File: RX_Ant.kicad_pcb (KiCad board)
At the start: 2 copper layers, 100 x 100 mm, 1630 parts, among them J1 CONN_COAXIAL, J10 CONN_COAXIAL, J11 CONN_COAXIAL, J12 CONN_01X05, J13 CONN_COAXIAL, J14 Conn_01x07, J15 CONN_COAXIAL, J16 CONN_01X01, J17 CONN_01X01, J18 CONN_01X01, J19 CONN_01X01, J2 CONN_COAXIAL, J20 CONN_01X01, J21 CONN_01X01, J22 CONN_01X01, J23 CONN_01X01, J24 CONN_COAXIAL, J25 CONN_COAXIAL, J26 CONN_COAXIAL, J27 CONN_COAXIAL, J28 CONN_COAXIAL, J29 CONN_COAXIAL, J3 CONN_COAXIAL, J30 CONN_COAXIAL, J31 CONN_COAXIAL, J32 CONN_COAXIAL, J34 CONN_COAXIAL, J35 CONN_COAXIAL, J37 CONN_COAXIAL, J4 CONN_COAXIAL, J5 CONN_COAXIAL, J6 CONN_COAXIAL, J8 CONN_COAXIAL, J9 CONN_COAXIAL

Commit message: minor errors fixed, sma edge should be changed
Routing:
- net Net-(J2-Pad1): track 16.4 -> 18.9 mm
- net Net-(J15-Pad1): track 25.4 -> 27.9 mm
- net Net-(J10-Pad1): track 17.3 -> 19.8 mm
- net Net-(J29-Pad1): track 28.0 -> 25.6 mm
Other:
- board text added: "(master)"
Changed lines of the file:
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@@
     (area 19.924999 24.924999 120.075001 125.075001)
     (thickness 1.6)
-    (drawings 35)
-    (tracks 1426)
+    (drawings 37)
+    (tracks 1428)
     (zones 0)
     (modules 1630)
@@
   )
   (setup
-    (last_trace_width 0.25)
+    (last_trace_width 2)
     (user_trace_width 0.5)
     (user_trace_width 1)
@@
     )
   )
+  (gr_text "(master)" (at 33 82.8) (layer F.SilkS)
+    (effects (font (size 1 1) (thickness 0.25) italic))
+  )
+  (gr_text "(master)" (at 34.2 34) (layer F.SilkS)
+    (effects (font (size 1 1) (thickness 0.25) italic))
+  )
   (gr_text "(HPF in)" (at 108 83 180) (layer F.SilkS)
     (effects (font (size 1 1) (thickness 0.25)))
@@
   (segment (start 80 86.65) (end 88.65 86.65) (width 2) (layer F.Cu) (net 2))
   (segment (start 88.65 86.65) (end 101.65 86.65) (width 2) (layer F.Cu) (net 2))
-  (segment (start 75 122.4) (end 75 120) (width 1) (layer F.Cu) (net 3))
+  (segment (start 75 122.5) (end 75 120) (width 2) (layer B.Cu) (net 3))
   (segment (start 75 120) (end 75 104.54) (width 2) (layer B.Cu) (net 3))
   (segment (start 75 104.54) (end 79.46 100.08) (width 2) (layer B.Cu) (net 3))
   (segment (start 84.54 100.08) (end 79.46 100.08) (width 2) (layer B.Cu) (net 3))
+  (segment (start 40 72.5) (end 40 70) (width 2) (layer B.Cu) (net 4))
   (segment (start 40 70) (end 40 65) (width 2) (layer B.Cu) (net 4))
   (segment (start 40 59) (end 40 65) (width 2.9) (layer B.Cu) (net 4))
   (segment (start 40 59) (end 43.5 55.5) (width 2.9) (layer B.Cu) (net 4))
   (segment (start 44 55.5) (end 43.5 55.5) (width 2.9) (layer B.Cu) (net 4))
+  (segment (start 100 72.5) (end 100 70) (width 2) (layer B.Cu) (net 5))
   (segment (start 100 70) (end 100 65) (width 2) (layer B.Cu) (net 5))
   (segment (start 100 61) (end 100 65) (width 2.9) (layer B.Cu) (net 5))
@@
   (segment (start 106.54 51.5) (end 46 51.5) (width 1) (layer F.Cu) (net 12))
   (via (at 46 51.5) (size 0.6) (drill 0.4) (layers F.Cu B.Cu) (net 12))
+  (segment (start 72.5 77.5) (end 72.5 80) (width 2) (layer B.Cu) (net 13))
   (segment (start 69.04 98.04) (end 70.46 98.04) (width 2) (layer B.Cu) (net 13))
   (segment (start 72.5 96) (end 72.5 80) (width 2) (layer B.Cu) (net 13))
@@
   (segment (start 60 93) (end 66.46 93) (width 1) (layer F.Cu) (net 20))
   (segment (start 66.46 93) (end 69.04 90.42) (width 1) (layer F.Cu) (net 20))
-  (segment (start 90 122.4) (end 90 120) (width 1) (layer F.Cu) (net 21))
   (segment (start 91.46 100.08) (end 96.54 100.08) (width 2) (layer B.Cu) (net 21))
   (segment (start 90 120) (end 90 101.54) (width 2) (layer B.Cu) (net 21))
   (segment (start 90 101.54) (end 91.46 100.08) (width 2) (layer B.Cu) (net 21))
-  (segment (start 70 72.4) (end 70 70) (width 2) (layer F.Cu) (net 22))
+  (segment (start 70 72.5) (end 70 70) (width 2) (layer B.Cu) (net 22))
   (segment (start 70 70) (end 70 65.2) (width 2) (layer B.Cu) (net 22))
   (segment (start 70 65.2) (end 70 56.5) (width 2.9) (layer B.Cu) (net 22))
   (segment (start 70 56.5) (end 69 55.5) (width 2) (layer B.Cu) (net 22))
-  (segment (start 105 122.4) (end 105 120) (width 1) (layer F.Cu) (net 23))
+  (segment (start 105 122.5) (end 105 120) (width 2) (layer B.Cu) (net 23))
   (segment (start 103.46 100.08) (end 108.54 100.08) (width 2) (layer B.Cu) (net 23))
   (segment (start 105 120) (end 105 101.62) (width 2) (layer B.Cu) (net 23))
   (segment (start 105 101.62) (end 103.46 100.08) (width 2) (layer B.Cu) (net 23))
+  (segment (start 60 122.5) (end 60 120) (width 2) (layer B.Cu) (net 24))
   (segment (start 60 120) (end 60 104.54) (width 2) (layer B.Cu) (net 24))
   (segment (start 60 104.54) (end 63.96 100.58) (width 2) (layer B.Cu) (net 24))
   (segment (start 63.96 100.58) (end 69.04 100.58) (width 2) (layer B.Cu) (net 24))
-  (segment (start 60 122.4) (end 60 120) (width 1) (layer F.Cu) (net 24))
-  (segment (start 100 77.5) (end 100 80) (width 1) (layer B.Cu) (net 25))
+  (segment (start 100 77.5) (end 100 80) (width 2) (layer B.Cu) (net 25))
   (segment (start 100 80) (end 100 97.54) (width 2) (layer B.Cu) (net 25))
   (segment (start 84.54 97.54) (end 79.46 97.54) (width 2) (layer B.Cu) (net 25))
@@
   (segment (start 100 97.54) (end 103.46 97.54) (width 2) (layer B.Cu) (net 25))
   (segment (start 91.46 97.54) (end 96.54 97.54) (width 2) (layer B.Cu) (net 25))
-  (segment (start 70 27.5) (end 70 30) (width 1) (layer B.Cu) (net 26))
+  (segment (start 70 27.5) (end 70 30) (width 2) (layer B.Cu) (net 26))
   (segment (start 75 41.3) (end 70 36.3) (width 2.9) (layer B.Cu) (net 26))
   (segment (start 70 36.3) (end 70 35) (width 2.9) (layer B.Cu) (net 26))

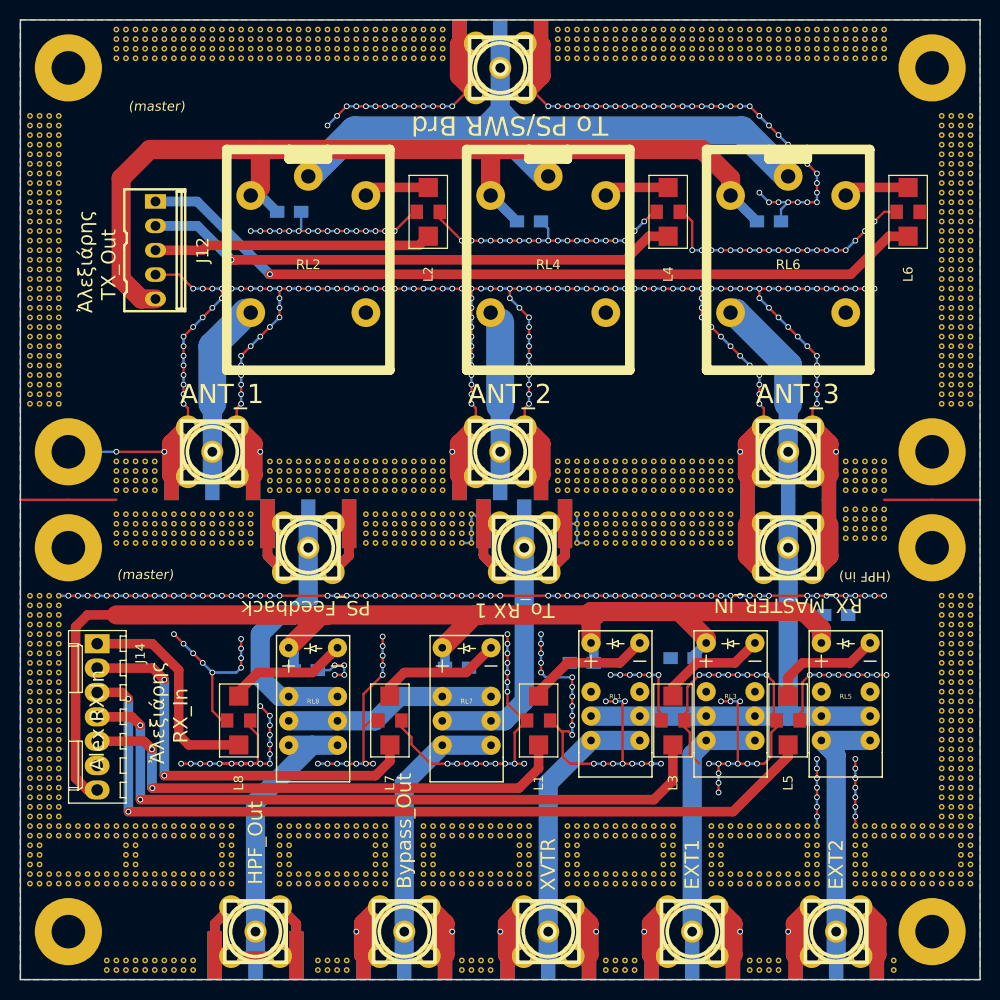
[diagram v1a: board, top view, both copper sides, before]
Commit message: V3.0, RX_master connector added, new stitching
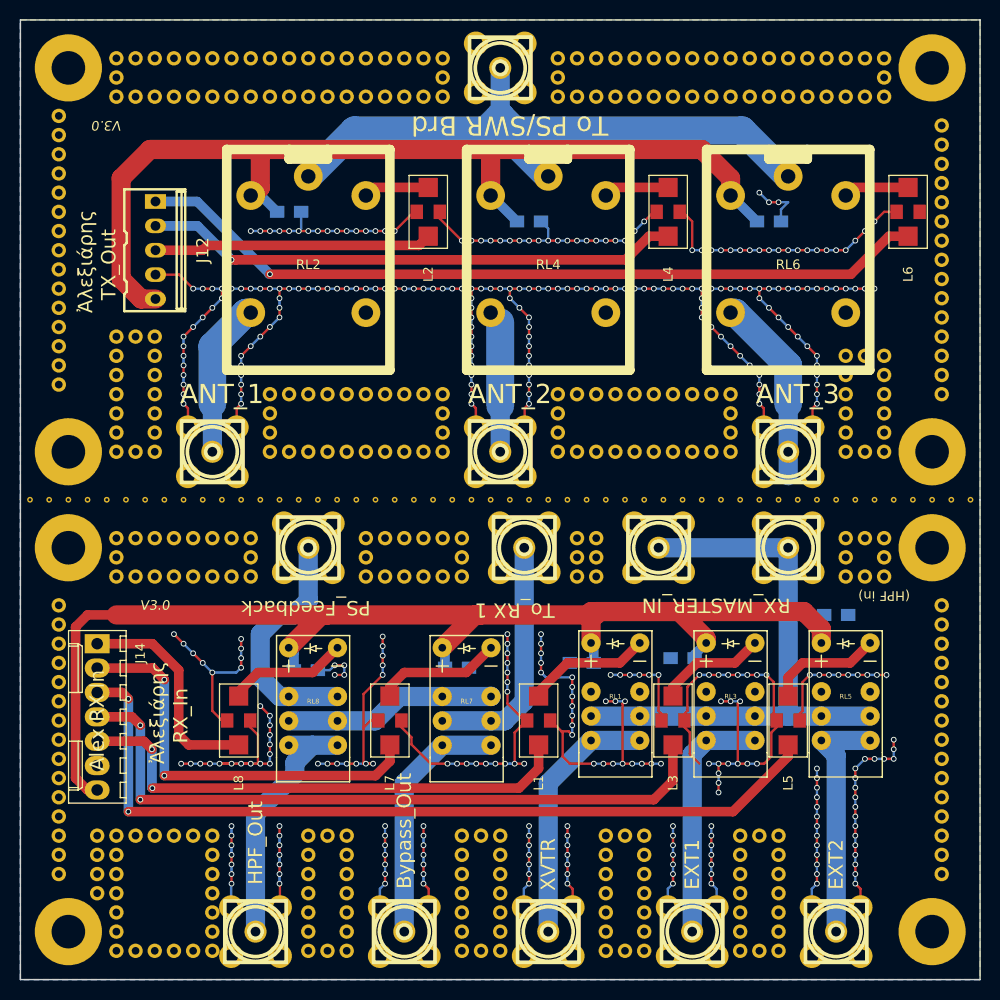
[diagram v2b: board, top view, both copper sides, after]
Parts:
- removed J11, J24, J25, J26, J27, J28, J29, J30, J31, J34, J35: CONN_COAXIAL, Connector_Coaxial:SMA_Amphenol_132289_EdgeMount
- removed the REF** at (67.0, 79.5)
- removed the REF** at (64.0, 76.5)
- removed the REF** at (90.0, 79.5)
- removed the REF** at (48.0, 28.0)
- removed the REF** at (47.0, 28.0)
- removed the REF** at (46.0, 28.0)
- removed the REF** at (45.0, 28.0)
- removed the REF** at (44.0, 28.0)
- removed the REF** at (43.0, 28.0)
- removed the REF** at (42.0, 28.0)
- removed the REF** at (41.0, 28.0)
- removed the REF** at (40.0, 28.0)
- removed the REF** at (39.0, 28.0)
- removed the REF** at (40.0, 79.5)
- removed the REF** at (38.0, 28.0)
- removed the REF** at (37.0, 28.0)
- removed the REF** at (36.0, 28.0)
- removed the REF** at (35.0, 28.0)
- removed the REF** at (34.0, 28.0)
- removed the REF** at (33.0, 28.0)
- removed the REF** at (32.0, 28.0)
- removed the REF** at (31.0, 28.0)
- removed the REF** at (30.0, 28.0)
- removed the REF** at (64.0, 27.0)
- removed the REF** at (40.0, 78.5)
- removed the REF** at (63.0, 27.0)
- removed the REF** at (62.0, 27.0)
- removed the REF** at (61.0, 27.0)
- removed the REF** at (60.0, 27.0)
- removed the REF** at (59.0, 27.0)
- removed the REF** at (58.0, 27.0)
- removed the REF** at (57.0, 27.0)
- removed the REF** at (56.0, 27.0)
- removed the REF** at (55.0, 27.0)
- removed the REF** at (54.0, 27.0)
- removed the REF** at (40.0, 77.5)
- removed the REF** at (53.0, 27.0)
- removed the REF** at (52.0, 27.0)
- removed the REF** at (51.0, 27.0)
- removed the REF** at (50.0, 27.0)
- removed the REF** at (49.0, 27.0)
- removed the REF** at (48.0, 27.0)
- removed the REF** at (47.0, 27.0)
- removed the REF** at (46.0, 27.0)
- removed the REF** at (45.0, 27.0)
- removed the REF** at (44.0, 27.0)
- removed the REF** at (40.0, 76.5)
- removed the REF** at (43.0, 27.0)
- removed the REF** at (42.0, 27.0)
- removed the REF** at (41.0, 27.0)
- removed the REF** at (40.0, 27.0)
- removed the REF** at (39.0, 27.0)
- removed the REF** at (38.0, 27.0)
- removed the REF** at (37.0, 27.0)
- removed the REF** at (36.0, 27.0)
- removed the REF** at (35.0, 27.0)
- removed the REF** at (34.0, 27.0)
- removed the REF** at (39.0, 79.5)
- removed the REF** at (33.0, 27.0)
- removed the REF** at (32.0, 27.0)
- removed the REF** at (31.0, 27.0)
- removed the REF** at (30.0, 27.0)
- removed the REF** at (64.0, 26.0)
- removed the REF** at (63.0, 26.0)
- removed the REF** at (62.0, 26.0)
- removed the REF** at (61.0, 26.0)
- removed the REF** at (60.0, 26.0)
- removed the REF** at (59.0, 26.0)
- removed the REF** at (38.0, 79.5)
- removed the REF** at (58.0, 26.0)
- removed the REF** at (57.0, 26.0)
- removed the REF** at (56.0, 26.0)
- removed the REF** at (55.0, 26.0)
- removed the REF** at (54.0, 26.0)
- removed the REF** at (53.0, 26.0)
- removed the REF** at (52.0, 26.0)
- removed the REF** at (51.0, 26.0)
- removed the REF** at (50.0, 26.0)
- removed the REF** at (49.0, 26.0)
- removed the REF** at (37.0, 79.5)
- removed the REF** at (48.0, 26.0)
- removed the REF** at (47.0, 26.0)
- removed the REF** at (46.0, 26.0)
- removed the REF** at (45.0, 26.0)
- removed the REF** at (44.0, 26.0)
- removed the REF** at (43.0, 26.0)
- removed the REF** at (42.0, 26.0)
- removed the REF** at (41.0, 26.0)
- removed the REF** at (40.0, 26.0)
- removed the REF** at (39.0, 26.0)
- removed the REF** at (36.0, 79.5)
- removed the REF** at (38.0, 26.0)
- removed the REF** at (37.0, 26.0)
- removed the REF** at (36.0, 26.0)
- removed the REF** at (35.0, 26.0)
- removed the REF** at (34.0, 26.0)
- removed the REF** at (33.0, 26.0)
- removed the REF** at (32.0, 26.0)
- removed the REF** at (31.0, 26.0)
- removed the REF** at (30.0, 26.0)
- removed the REF** at (24.0, 115.0)
- removed the REF** at (39.0, 78.5)
- removed the REF** at (23.0, 115.0)
- removed the REF** at (22.0, 115.0)
- removed the REF** at (21.0, 115.0)
- removed the REF** at (23.0, 114.0)
- removed the REF** at (22.0, 114.0)
- removed the REF** at (21.0, 114.0)
- removed the REF** at (22.0, 113.0)
- removed the REF** at (21.0, 113.0)
- removed the REF** at (22.0, 112.0)
- removed the REF** at (65.0, 77.5)
- removed the REF** at (38.0, 78.5)
- removed the REF** at (21.0, 112.0)
- removed the REF** at (22.0, 111.0)
- removed the REF** at (21.0, 111.0)
- removed the REF** at (23.0, 110.0)
- removed the REF** at (22.0, 110.0)
- removed the REF** at (21.0, 110.0)
- removed the REF** at (24.0, 109.0)
- removed the REF** at (23.0, 109.0)
- removed the REF** at (22.0, 109.0)
- removed the REF** at (37.0, 78.5)
- removed the REF** at (21.0, 109.0)
- removed the REF** at (23.0, 108.0)
- removed the REF** at (22.0, 108.0)
- removed the REF** at (21.0, 108.0)
- removed the REF** at (24.0, 107.0)
- removed the REF** at (23.0, 107.0)
- removed the REF** at (22.0, 107.0)
- removed the REF** at (21.0, 107.0)
- removed the REF** at (36.0, 78.5)
- removed the REF** at (23.0, 106.0)
- removed the REF** at (22.0, 106.0)
- removed the REF** at (21.0, 106.0)
- removed the REF** at (24.0, 105.0)
- removed the REF** at (23.0, 105.0)
- removed the REF** at (22.0, 105.0)
- removed the REF** at (21.0, 105.0)
- removed the REF** at (23.0, 104.0)
- removed the REF** at (22.0, 104.0)
- removed the REF** at (39.0, 77.5)
- removed the REF** at (21.0, 104.0)
- removed the REF** at (24.0, 103.0)
- removed the REF** at (23.0, 103.0)
- removed the REF** at (22.0, 103.0)
- removed the REF** at (21.0, 103.0)
- removed the REF** at (23.0, 102.0)
- removed the REF** at (22.0, 102.0)
- removed the REF** at (21.0, 102.0)
- removed the REF** at (24.0, 101.0)
- removed the REF** at (38.0, 77.5)
- removed the REF** at (23.0, 101.0)
- removed the REF** at (22.0, 101.0)
- removed the REF** at (21.0, 101.0)
- removed the REF** at (23.0, 100.0)
- removed the REF** at (22.0, 100.0)
- removed the REF** at (21.0, 100.0)
- removed the REF** at (24.0, 99.0)
- removed the REF** at (23.0, 99.0)
- removed the REF** at (22.0, 99.0)
- removed the REF** at (37.0, 77.5)
- removed the REF** at (21.0, 99.0)
- removed the REF** at (23.0, 98.0)
- removed the REF** at (22.0, 98.0)
- removed the REF** at (21.0, 98.0)
- removed the REF** at (24.0, 97.0)
- removed the REF** at (23.0, 97.0)
- removed the REF** at (22.0, 97.0)
- removed the REF** at (21.0, 97.0)
- removed the REF** at (36.0, 77.5)
- removed the REF** at (23.0, 96.0)
- removed the REF** at (22.0, 96.0)
- removed the REF** at (21.0, 96.0)
- removed the REF** at (24.0, 95.0)
- removed the REF** at (23.0, 95.0)
- removed the REF** at (22.0, 95.0)
- removed the REF** at (21.0, 95.0)
- removed the REF** at (23.0, 94.0)
- removed the REF** at (22.0, 94.0)
- removed the REF** at (39.0, 76.5)
- removed the REF** at (21.0, 94.0)
- removed the REF** at (24.0, 93.0)
- removed the REF** at (23.0, 93.0)
- removed the REF** at (22.0, 93.0)
- removed the REF** at (21.0, 93.0)
- removed the REF** at (23.0, 92.0)
- removed the REF** at (22.0, 92.0)
- removed the REF** at (21.0, 92.0)
- removed the REF** at (24.0, 91.0)
- removed the REF** at (38.0, 76.5)
- removed the REF** at (23.0, 91.0)
- removed the REF** at (22.0, 91.0)
- removed the REF** at (21.0, 91.0)
- removed the REF** at (23.0, 90.0)
- removed the REF** at (22.0, 90.0)
- removed the REF** at (21.0, 90.0)
- removed the REF** at (24.0, 89.0)
- removed the REF** at (23.0, 89.0)
- removed the REF** at (22.0, 89.0)
- removed the REF** at (37.0, 76.5)
- removed the REF** at (21.0, 89.0)
- removed the REF** at (23.0, 88.0)
- removed the REF** at (22.0, 88.0)
- removed the REF** at (21.0, 88.0)
- removed the REF** at (24.0, 87.0)
- removed the REF** at (23.0, 87.0)
- removed the REF** at (22.0, 87.0)
- removed the REF** at (21.0, 87.0)
- removed the REF** at (64.0, 77.5)
- removed the REF** at (36.0, 76.5)
- removed the REF** at (23.0, 86.0)
- removed the REF** at (22.0, 86.0)
- removed the REF** at (21.0, 86.0)
- removed the REF** at (24.0, 85.0)
- removed the REF** at (23.0, 85.0)
- removed the REF** at (22.0, 85.0)
- removed the REF** at (21.0, 85.0)
- removed the REF** at (24.0, 65.0)
- removed the REF** at (23.0, 65.0)
- removed the REF** at (22.0, 65.0)
- removed the REF** at (35.0, 76.5)
- removed the REF** at (21.0, 65.0)
- removed the REF** at (24.0, 64.0)
- removed the REF** at (23.0, 64.0)
- removed the REF** at (22.0, 64.0)
- removed the REF** at (21.0, 64.0)
- removed the REF** at (23.0, 63.0)
- removed the REF** at (22.0, 63.0)
- removed the REF** at (21.0, 63.0)
- removed the REF** at (24.0, 62.0)
- removed the REF** at (30.0, 76.5)
- removed the REF** at (23.0, 62.0)
- removed the REF** at (22.0, 62.0)
- removed the REF** at (21.0, 62.0)
- removed the REF** at (23.0, 61.0)
- removed the REF** at (22.0, 61.0)
- removed the REF** at (21.0, 61.0)
- removed the REF** at (24.0, 60.0)
- removed the REF** at (23.0, 60.0)
- removed the REF** at (22.0, 60.0)
- removed the REF** at (31.0, 76.5)
- removed the REF** at (21.0, 60.0)
- removed the REF** at (23.0, 59.0)
- removed the REF** at (22.0, 59.0)
- removed the REF** at (21.0, 59.0)
- removed the REF** at (24.0, 58.0)
- removed the REF** at (23.0, 58.0)
- removed the REF** at (22.0, 58.0)
- removed the REF** at (21.0, 58.0)
- removed the REF** at (32.0, 76.5)
- removed the REF** at (23.0, 57.0)
- removed the REF** at (22.0, 57.0)
- removed the REF** at (21.0, 57.0)
- removed the REF** at (24.0, 56.0)
- removed the REF** at (23.0, 56.0)
- removed the REF** at (22.0, 56.0)
- removed the REF** at (21.0, 56.0)
- removed the REF** at (23.0, 55.0)
- removed the REF** at (22.0, 55.0)
- removed the REF** at (33.0, 76.5)
- removed the REF** at (21.0, 55.0)
- removed the REF** at (24.0, 54.0)
- removed the REF** at (23.0, 54.0)
- removed the REF** at (22.0, 54.0)
- removed the REF** at (21.0, 54.0)
- removed the REF** at (23.0, 53.0)
- removed the REF** at (22.0, 53.0)
- removed the REF** at (21.0, 53.0)
- removed the REF** at (24.0, 52.0)
- removed the REF** at (34.0, 76.5)
- removed the REF** at (23.0, 52.0)
- removed the REF** at (22.0, 52.0)
- removed the REF** at (21.0, 52.0)
- removed the REF** at (23.0, 51.0)
- removed the REF** at (22.0, 51.0)
- removed the REF** at (21.0, 51.0)
- removed the REF** at (24.0, 50.0)
- removed the REF** at (23.0, 50.0)
- removed the REF** at (22.0, 50.0)
- removed the REF** at (35.0, 77.5)
- removed the REF** at (21.0, 50.0)
- removed the REF** at (23.0, 49.0)
- removed the REF** at (22.0, 49.0)
- removed the REF** at (21.0, 49.0)
- removed the REF** at (24.0, 48.0)
- removed the REF** at (23.0, 48.0)
- removed the REF** at (22.0, 48.0)
- removed the REF** at (21.0, 48.0)
- removed the REF** at (30.0, 77.5)
- removed the REF** at (23.0, 47.0)
- removed the REF** at (22.0, 47.0)
- removed the REF** at (21.0, 47.0)
- removed the REF** at (24.0, 46.0)
- removed the REF** at (23.0, 46.0)
- removed the REF** at (22.0, 46.0)
- removed the REF** at (21.0, 46.0)
- removed the REF** at (23.0, 45.0)
- removed the REF** at (22.0, 45.0)
- removed the REF** at (31.0, 77.5)
- removed the REF** at (21.0, 45.0)
- removed the REF** at (24.0, 44.0)
- removed the REF** at (23.0, 44.0)
- removed the REF** at (22.0, 44.0)
- removed the REF** at (21.0, 44.0)
- removed the REF** at (23.0, 43.0)
- removed the REF** at (22.0, 43.0)
- removed the REF** at (21.0, 43.0)
- removed the REF** at (24.0, 42.0)
- removed the REF** at (65.0, 78.5)
- removed the REF** at (32.0, 77.5)
- removed the REF** at (23.0, 42.0)
- removed the REF** at (22.0, 42.0)
- removed the REF** at (21.0, 42.0)
- removed the REF** at (23.0, 41.0)
- removed the REF** at (22.0, 41.0)
- removed the REF** at (21.0, 41.0)
- removed the REF** at (24.0, 40.0)
- removed the REF** at (23.0, 40.0)
- removed the REF** at (22.0, 40.0)
- removed the REF** at (33.0, 77.5)
- removed the REF** at (21.0, 40.0)
- removed the REF** at (23.0, 39.0)
- removed the REF** at (22.0, 39.0)
- removed the REF** at (21.0, 39.0)
- removed the REF** at (24.0, 38.0)
- removed the REF** at (23.0, 38.0)
- removed the REF** at (22.0, 38.0)
- removed the REF** at (21.0, 38.0)
- removed the REF** at (34.0, 77.5)
- removed the REF** at (23.0, 37.0)
- removed the REF** at (22.0, 37.0)
- removed the REF** at (21.0, 37.0)
- removed the REF** at (24.0, 36.0)
- removed the REF** at (23.0, 36.0)
- removed the REF** at (22.0, 36.0)
- removed the REF** at (21.0, 36.0)
- removed the REF** at (23.0, 35.0)
- removed the REF** at (22.0, 35.0)
- removed the REF** at (35.0, 78.5)
- removed the REF** at (21.0, 35.0)
- removed the REF** at (119.0, 115.0)
- removed the REF** at (118.0, 115.0)
- removed the REF** at (117.0, 115.0)
- removed the REF** at (116.0, 115.0)
- removed the REF** at (119.0, 114.0)
- removed the REF** at (118.0, 114.0)
- removed the REF** at (117.0, 114.0)
- removed the REF** at (119.0, 113.0)
- removed the REF** at (30.0, 78.5)
- removed the REF** at (118.0, 113.0)
- removed the REF** at (119.0, 112.0)
- removed the REF** at (118.0, 112.0)
- removed the REF** at (119.0, 111.0)
- removed the REF** at (118.0, 111.0)
- removed the REF** at (119.0, 110.0)
- removed the REF** at (118.0, 110.0)
- removed the REF** at (117.0, 110.0)
- removed the REF** at (119.0, 109.0)
- removed the REF** at (31.0, 78.5)
- removed the REF** at (118.0, 109.0)
- removed the REF** at (117.0, 109.0)
- removed the REF** at (116.0, 109.0)
- removed the REF** at (119.0, 108.0)
- removed the REF** at (118.0, 108.0)
- removed the REF** at (117.0, 108.0)
- removed the REF** at (119.0, 107.0)
- removed the REF** at (118.0, 107.0)
- removed the REF** at (117.0, 107.0)
- removed the REF** at (32.0, 78.5)
- removed the REF** at (116.0, 107.0)
- removed the REF** at (119.0, 106.0)
- removed the REF** at (118.0, 106.0)
- removed the REF** at (117.0, 106.0)
- removed the REF** at (119.0, 105.0)
- removed the REF** at (118.0, 105.0)
- removed the REF** at (117.0, 105.0)
- removed the REF** at (116.0, 105.0)
- removed the REF** at (119.0, 104.0)
- removed the REF** at (33.0, 78.5)
- removed the REF** at (118.0, 104.0)
- removed the REF** at (117.0, 104.0)
- removed the REF** at (119.0, 103.0)
- removed the REF** at (118.0, 103.0)
- removed the REF** at (117.0, 103.0)
- removed the REF** at (116.0, 103.0)
- removed the REF** at (119.0, 102.0)
- removed the REF** at (118.0, 102.0)
- removed the REF** at (117.0, 102.0)
- removed the REF** at (34.0, 78.5)
- removed the REF** at (119.0, 101.0)
- removed the REF** at (118.0, 101.0)
- removed the REF** at (117.0, 101.0)
- removed the REF** at (116.0, 101.0)
- removed the REF** at (119.0, 100.0)
- removed the REF** at (118.0, 100.0)
- removed the REF** at (117.0, 100.0)
- removed the REF** at (119.0, 99.0)
- removed the REF** at (35.0, 79.5)
- removed the REF** at (118.0, 99.0)
- removed the REF** at (117.0, 99.0)
- removed the REF** at (116.0, 99.0)
- removed the REF** at (119.0, 98.0)
- removed the REF** at (118.0, 98.0)
- removed the REF** at (117.0, 98.0)
- removed the REF** at (119.0, 97.0)
- removed the REF** at (118.0, 97.0)
- removed the REF** at (117.0, 97.0)
- removed the REF** at (64.0, 78.5)
- removed the REF** at (30.0, 79.5)
- removed the REF** at (116.0, 97.0)
- removed the REF** at (119.0, 96.0)
- removed the REF** at (118.0, 96.0)
- removed the REF** at (117.0, 96.0)
- removed the REF** at (119.0, 95.0)
- removed the REF** at (118.0, 95.0)
- removed the REF** at (117.0, 95.0)
- removed the REF** at (116.0, 95.0)
- removed the REF** at (119.0, 94.0)
- removed the REF** at (31.0, 79.5)
- removed the REF** at (118.0, 94.0)
- removed the REF** at (117.0, 94.0)
- removed the REF** at (119.0, 93.0)
- removed the REF** at (118.0, 93.0)
- removed the REF** at (117.0, 93.0)
- removed the REF** at (116.0, 93.0)
- removed the REF** at (119.0, 92.0)
- removed the REF** at (118.0, 92.0)
- removed the REF** at (117.0, 92.0)
- removed the REF** at (32.0, 79.5)
- removed the REF** at (119.0, 91.0)
- removed the REF** at (118.0, 91.0)
- removed the REF** at (117.0, 91.0)
- removed the REF** at (116.0, 91.0)
- removed the REF** at (119.0, 90.0)
- removed the REF** at (118.0, 90.0)
- removed the REF** at (117.0, 90.0)
- removed the REF** at (119.0, 89.0)
- removed the REF** at (33.0, 79.5)
- removed the REF** at (118.0, 89.0)
- removed the REF** at (117.0, 89.0)
- removed the REF** at (116.0, 89.0)
- removed the REF** at (119.0, 88.0)
- removed the REF** at (118.0, 88.0)
- removed the REF** at (117.0, 88.0)
- removed the REF** at (119.0, 87.0)
- removed the REF** at (118.0, 87.0)
- removed the REF** at (117.0, 87.0)
- removed the REF** at (34.0, 79.5)
- removed the REF** at (116.0, 87.0)
- removed the REF** at (119.0, 86.0)
- removed the REF** at (118.0, 86.0)
- removed the REF** at (117.0, 86.0)
- removed the REF** at (119.0, 85.0)
- removed the REF** at (118.0, 85.0)
- removed the REF** at (117.0, 85.0)
- removed the REF** at (116.0, 85.0)
- removed the REF** at (119.0, 65.0)
- removed the REF** at (94.0, 79.5)
- removed the REF** at (118.0, 65.0)
- removed the REF** at (117.0, 65.0)
- removed the REF** at (116.0, 65.0)
- removed the REF** at (119.0, 64.0)
- removed the REF** at (118.0, 64.0)
- removed the REF** at (117.0, 64.0)
- removed the REF** at (119.0, 63.0)
- removed the REF** at (118.0, 63.0)
- removed the REF** at (117.0, 63.0)
- removed the REF** at (93.0, 79.5)
- removed the REF** at (116.0, 63.0)
- removed the REF** at (119.0, 62.0)
- removed the REF** at (118.0, 62.0)
- removed the REF** at (117.0, 62.0)
- removed the REF** at (119.0, 61.0)
- removed the REF** at (118.0, 61.0)
- removed the REF** at (117.0, 61.0)
- removed the REF** at (116.0, 61.0)
- removed the REF** at (119.0, 60.0)
- removed the REF** at (92.0, 79.5)
- removed the REF** at (118.0, 60.0)
- removed the REF** at (117.0, 60.0)
- removed the REF** at (119.0, 59.0)
- removed the REF** at (118.0, 59.0)
- removed the REF** at (117.0, 59.0)
- removed the REF** at (116.0, 59.0)
- removed the REF** at (119.0, 58.0)
- removed the REF** at (118.0, 58.0)
- removed the REF** at (117.0, 58.0)
- removed the REF** at (91.0, 79.5)
- removed the REF** at (119.0, 57.0)
- removed the REF** at (118.0, 57.0)
- removed the REF** at (117.0, 57.0)
- removed the REF** at (116.0, 57.0)
- removed the REF** at (119.0, 56.0)
- removed the REF** at (118.0, 56.0)
- removed the REF** at (117.0, 56.0)
- removed the REF** at (119.0, 55.0)
- removed the REF** at (94.0, 78.5)
- removed the REF** at (118.0, 55.0)
- removed the REF** at (117.0, 55.0)
- removed the REF** at (116.0, 55.0)
- removed the REF** at (119.0, 54.0)
- removed the REF** at (118.0, 54.0)
- removed the REF** at (117.0, 54.0)
- removed the REF** at (119.0, 53.0)
- removed the REF** at (118.0, 53.0)
- removed the REF** at (117.0, 53.0)
- removed the REF** at (65.0, 79.5)
- removed the REF** at (93.0, 78.5)
- removed the REF** at (116.0, 53.0)
- removed the REF** at (119.0, 52.0)
- removed the REF** at (118.0, 52.0)
- removed the REF** at (117.0, 52.0)
- removed the REF** at (119.0, 51.0)
- removed the REF** at (118.0, 51.0)
- removed the REF** at (117.0, 51.0)
- removed the REF** at (116.0, 51.0)
- removed the REF** at (119.0, 50.0)
- removed the REF** at (92.0, 78.5)
- removed the REF** at (118.0, 50.0)
- removed the REF** at (117.0, 50.0)
- removed the REF** at (119.0, 49.0)
- removed the REF** at (118.0, 49.0)
- removed the REF** at (117.0, 49.0)
- removed the REF** at (116.0, 49.0)
- removed the REF** at (119.0, 48.0)
- removed the REF** at (118.0, 48.0)
- removed the REF** at (117.0, 48.0)
- removed the REF** at (91.0, 78.5)
- removed the REF** at (119.0, 47.0)
- removed the REF** at (118.0, 47.0)
- removed the REF** at (117.0, 47.0)
- removed the REF** at (116.0, 47.0)
- removed the REF** at (119.0, 46.0)
- removed the REF** at (118.0, 46.0)
- removed the REF** at (117.0, 46.0)
- removed the REF** at (119.0, 45.0)
- removed the REF** at (94.0, 77.5)
- removed the REF** at (118.0, 45.0)
- removed the REF** at (117.0, 45.0)
- removed the REF** at (116.0, 45.0)
- removed the REF** at (119.0, 44.0)
- removed the REF** at (118.0, 44.0)
- removed the REF** at (117.0, 44.0)
- removed the REF** at (119.0, 43.0)
- removed the REF** at (118.0, 43.0)
- removed the REF** at (117.0, 43.0)
- removed the REF** at (93.0, 77.5)
- removed the REF** at (116.0, 43.0)
- removed the REF** at (119.0, 42.0)
- removed the REF** at (118.0, 42.0)
- removed the REF** at (117.0, 42.0)
- removed the REF** at (119.0, 41.0)
- removed the REF** at (118.0, 41.0)
- removed the REF** at (117.0, 41.0)
- removed the REF** at (116.0, 41.0)
- removed the REF** at (119.0, 40.0)
- removed the REF** at (92.0, 77.5)
- removed the REF** at (118.0, 40.0)
- removed the REF** at (117.0, 40.0)
- removed the REF** at (119.0, 39.0)
- removed the REF** at (118.0, 39.0)
- removed the REF** at (117.0, 39.0)
- removed the REF** at (116.0, 39.0)
- removed the REF** at (119.0, 38.0)
- removed the REF** at (118.0, 38.0)
- removed the REF** at (117.0, 38.0)
- removed the REF** at (91.0, 77.5)
- removed the REF** at (119.0, 37.0)
- removed the REF** at (118.0, 37.0)
- removed the REF** at (117.0, 37.0)
- removed the REF** at (116.0, 37.0)
- removed the REF** at (119.0, 36.0)
- removed the REF** at (118.0, 36.0)
- removed the REF** at (117.0, 36.0)
- removed the REF** at (119.0, 35.0)
- removed the REF** at (94.0, 76.5)
- removed the REF** at (118.0, 35.0)
- removed the REF** at (117.0, 35.0)
- removed the REF** at (116.0, 35.0)
- removed the REF** at (93.0, 76.5)
- removed the REF** at (92.0, 76.5)
- removed the REF** at (64.0, 79.5)
- removed the REF** at (91.0, 76.5)
- removed the REF** at (44.0, 79.5)
- removed the REF** at (43.0, 79.5)
- removed the REF** at (42.0, 79.5)
- removed the REF** at (41.0, 79.5)
- removed the REF** at (44.0, 78.5)
- removed the REF** at (43.0, 78.5)
- removed the REF** at (42.0, 78.5)
- removed the REF** at (41.0, 78.5)
- removed the REF** at (44.0, 77.5)
- removed the REF** at (60.0, 79.5)
- removed the REF** at (43.0, 77.5)
- removed the REF** at (42.0, 77.5)
- removed the REF** at (41.0, 77.5)
- removed the REF** at (44.0, 76.5)
- removed the REF** at (43.0, 76.5)
- removed the REF** at (42.0, 76.5)
- removed the REF** at (41.0, 76.5)
- removed the REF** at (29.0, 115.0)
- removed the REF** at (28.0, 115.0)
- removed the REF** at (27.0, 115.0)
- removed the REF** at (59.0, 79.5)
- removed the REF** at (26.0, 115.0)
- removed the REF** at (30.0, 115.0)
- removed the REF** at (31.0, 115.0)
- removed the REF** at (31.0, 109.0)
- removed the REF** at (31.0, 110.0)
- removed the REF** at (31.0, 111.0)
- removed the REF** at (31.0, 112.0)
- removed the REF** at (31.0, 113.0)
- removed the REF** at (31.0, 114.0)
- removed the REF** at (58.0, 79.5)
- removed the REF** at (30.0, 109.0)
- removed the REF** at (26.0, 114.0)
- removed the REF** at (26.0, 110.0)
- removed the REF** at (26.0, 109.0)
- removed the REF** at (27.0, 109.0)
- removed the REF** at (28.0, 109.0)
- removed the REF** at (27.0, 110.0)
- removed the REF** at (27.0, 114.0)
- removed the REF** at (66.0, 79.5)
- removed the REF** at (57.0, 79.5)
- removed the REF** at (42.0, 115.0)
- removed the REF** at (41.0, 115.0)
- removed the REF** at (40.0, 115.0)
- removed the REF** at (39.0, 115.0)
- removed the REF** at (38.0, 115.0)
- removed the REF** at (37.0, 115.0)
- removed the REF** at (36.0, 115.0)
- removed the REF** at (35.0, 115.0)
- removed the REF** at (34.0, 115.0)
- removed the REF** at (56.0, 79.5)
- removed the REF** at (33.0, 115.0)
- removed the REF** at (32.0, 115.0)
- removed the REF** at (42.0, 114.0)
- removed the REF** at (41.0, 114.0)
- removed the REF** at (39.0, 114.0)
- removed the REF** at (38.0, 114.0)
- removed the REF** at (37.0, 114.0)
- removed the REF** at (36.0, 114.0)
- removed the REF** at (35.0, 114.0)
- removed the REF** at (61.0, 79.5)
- removed the REF** at (34.0, 114.0)
- removed the REF** at (33.0, 114.0)
- removed the REF** at (32.0, 114.0)
- removed the REF** at (29.0, 114.0)
- removed the REF** at (42.0, 113.0)
- removed the REF** at (41.0, 113.0)
- removed the REF** at (32.0, 113.0)
- removed the REF** at (42.0, 112.0)
- removed the REF** at (41.0, 112.0)
- removed the REF** at (32.0, 112.0)
- removed the REF** at (60.0, 78.5)
- removed the REF** at (42.0, 111.0)
- removed the REF** at (41.0, 111.0)
- removed the REF** at (32.0, 111.0)
- removed the REF** at (42.0, 110.0)
- removed the REF** at (41.0, 110.0)
- removed the REF** at (39.0, 110.0)
- removed the REF** at (37.0, 110.0)
- removed the REF** at (59.0, 78.5)
- removed the REF** at (35.0, 110.0)
- removed the REF** at (33.0, 110.0)
- removed the REF** at (29.0, 110.0)
- removed the REF** at (42.0, 109.0)
- removed the REF** at (41.0, 109.0)
- removed the REF** at (40.0, 109.0)
- removed the REF** at (39.0, 109.0)
- removed the REF** at (38.0, 109.0)
- removed the REF** at (58.0, 78.5)
- removed the REF** at (37.0, 109.0)
- removed the REF** at (36.0, 109.0)
- removed the REF** at (35.0, 109.0)
- removed the REF** at (34.0, 109.0)
- removed the REF** at (33.0, 109.0)
- removed the REF** at (32.0, 109.0)
- removed the REF** at (29.0, 109.0)
- removed the REF** at (47.0, 109.0)
- removed the REF** at (48.0, 109.0)
- removed the REF** at (49.0, 109.0)
- removed the REF** at (57.0, 78.5)
- removed the REF** at (50.0, 109.0)
- removed the REF** at (51.0, 109.0)
- removed the REF** at (52.0, 109.0)
- removed the REF** at (53.0, 109.0)
- removed the REF** at (54.0, 109.0)
- removed the REF** at (55.0, 109.0)
- removed the REF** at (56.0, 109.0)
- removed the REF** at (57.0, 109.0)
- removed the REF** at (58.0, 109.0)
- removed the REF** at (47.0, 110.0)
- removed the REF** at (56.0, 78.5)
- removed the REF** at (48.0, 110.0)
- removed the REF** at (49.0, 110.0)
- removed the REF** at (51.0, 110.0)
- removed the REF** at (53.0, 110.0)
- removed the REF** at (55.0, 110.0)
- removed the REF** at (56.0, 110.0)
- removed the REF** at (57.0, 110.0)
- removed the REF** at (61.0, 78.5)
- removed the REF** at (58.0, 110.0)
- removed the REF** at (47.0, 111.0)
- removed the REF** at (48.0, 111.0)
- removed the REF** at (57.0, 111.0)
- removed the REF** at (58.0, 111.0)
- removed the REF** at (47.0, 112.0)
- removed the REF** at (48.0, 112.0)
- removed the REF** at (57.0, 112.0)
- removed the REF** at (58.0, 112.0)
- removed the REF** at (47.0, 113.0)
- removed the REF** at (60.0, 77.5)
- removed the REF** at (48.0, 113.0)
- removed the REF** at (57.0, 113.0)
- removed the REF** at (58.0, 113.0)
- removed the REF** at (47.0, 114.0)
- removed the REF** at (48.0, 114.0)
- removed the REF** at (49.0, 114.0)
- removed the REF** at (51.0, 114.0)
- removed the REF** at (52.0, 114.0)
- removed the REF** at (53.0, 114.0)
- removed the REF** at (67.0, 78.5)
- removed the REF** at (59.0, 77.5)
- removed the REF** at (55.0, 114.0)
- removed the REF** at (56.0, 114.0)
- removed the REF** at (57.0, 114.0)
- removed the REF** at (58.0, 114.0)
- removed the REF** at (47.0, 115.0)
- removed the REF** at (48.0, 115.0)
- removed the REF** at (49.0, 115.0)
- removed the REF** at (50.0, 115.0)
- removed the REF** at (51.0, 115.0)
- removed the REF** at (58.0, 77.5)
- removed the REF** at (52.0, 115.0)
- removed the REF** at (53.0, 115.0)
- removed the REF** at (54.0, 115.0)
- removed the REF** at (55.0, 115.0)
- removed the REF** at (56.0, 115.0)
- removed the REF** at (57.0, 115.0)
- removed the REF** at (58.0, 115.0)
- removed the REF** at (111.0, 124.0)
- removed the REF** at (99.0, 124.0)
- removed the REF** at (98.0, 124.0)
- removed the REF** at (57.0, 77.5)
- removed the REF** at (97.0, 124.0)
- removed the REF** at (96.0, 124.0)
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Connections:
- J8 pad 1: Net-(J32-Pad1) -> Net-(J8-Pad1)
- J9 pad 1: Net-(J28-Pad1) -> Net-(J32-Pad1)
- RL1 pad 4: Net-(J28-Pad1) -> Net-(J32-Pad1)
- RL1 pad 9: Net-(J28-Pad1) -> Net-(J32-Pad1)
- RL3 pad 4: Net-(J28-Pad1) -> Net-(J32-Pad1)
- RL3 pad 9: Net-(J28-Pad1) -> Net-(J32-Pad1)
- RL5 pad 4: Net-(J28-Pad1) -> Net-(J32-Pad1)
- RL5 pad 9: Net-(J28-Pad1) -> Net-(J32-Pad1)
- RL7 pad 5: Net-(J32-Pad1) -> Net-(J8-Pad1)
- RL7 pad 8: Net-(J32-Pad1) -> Net-(J8-Pad1)
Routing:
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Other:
- board text added: "V3.0"
- board text removed: "(master)"

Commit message: upgrate to Kicad 5.0n, new up to date Gerber
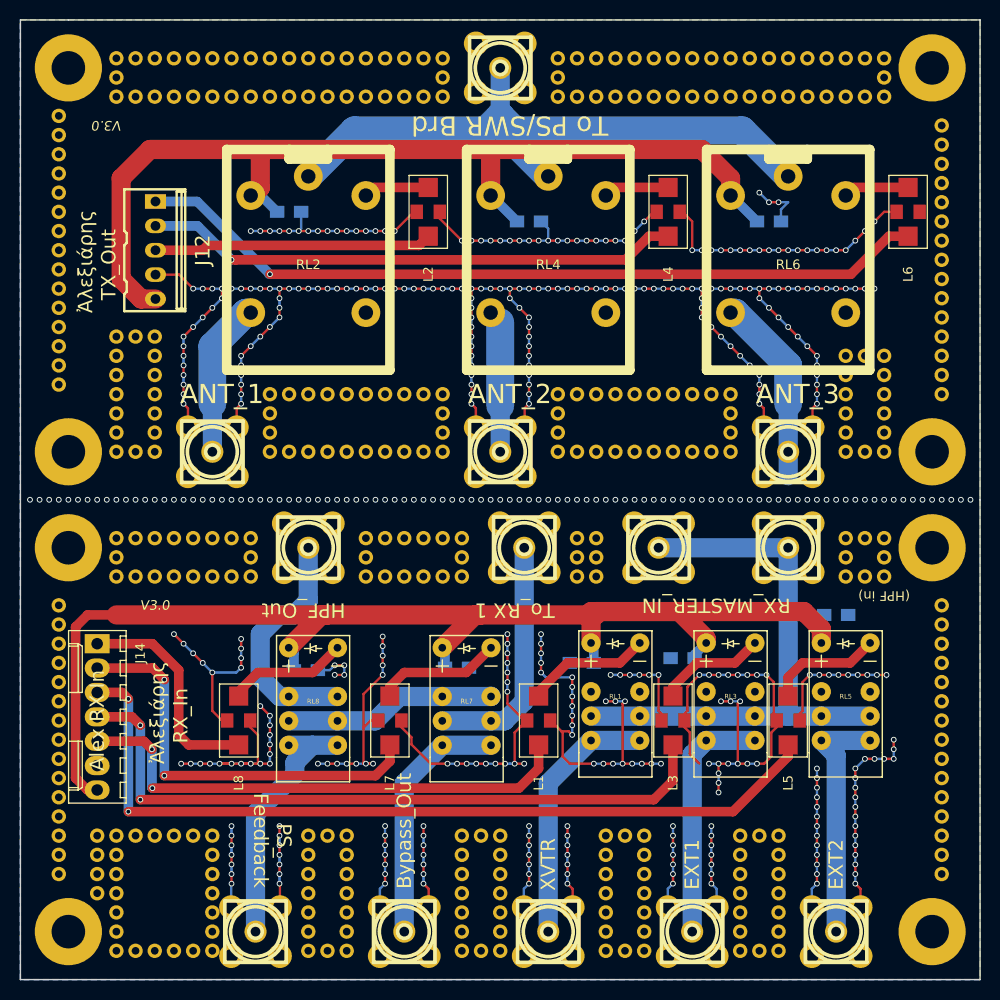
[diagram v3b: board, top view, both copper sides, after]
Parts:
- removed the REF** at (119.0, 75.0)
- removed the REF** at (101.0, 75.0)
- removed the REF** at (99.0, 75.0)
- removed the REF** at (97.0, 75.0)
- removed the REF** at (95.0, 75.0)
- removed the REF** at (93.0, 75.0)
- removed the REF** at (91.0, 75.0)
- removed the REF** at (89.0, 75.0)
- removed the REF** at (87.0, 75.0)
- removed the REF** at (85.0, 75.0)
- removed the REF** at (83.0, 75.0)
- removed the REF** at (117.0, 75.0)
- removed the REF** at (81.0, 75.0)
- removed the REF** at (79.0, 75.0)
- removed the REF** at (77.0, 75.0)
- removed the REF** at (75.0, 75.0)
- removed the REF** at (73.0, 75.0)
- removed the REF** at (71.0, 75.0)
- removed the REF** at (69.0, 75.0)
- removed the REF** at (67.0, 75.0)
- removed the REF** at (65.0, 75.0)
- removed the REF** at (63.0, 75.0)
- removed the REF** at (115.0, 75.0)
- removed the REF** at (61.0, 75.0)
- removed the REF** at (59.0, 75.0)
- removed the REF** at (57.0, 75.0)
- removed the REF** at (55.0, 75.0)
- removed the REF** at (53.0, 75.0)
- removed the REF** at (51.0, 75.0)
- removed the REF** at (49.0, 75.0)
- removed the REF** at (47.0, 75.0)
- removed the REF** at (45.0, 75.0)
- removed the REF** at (43.0, 75.0)
- removed the REF** at (113.0, 75.0)
- removed the REF** at (41.0, 75.0)
- removed the REF** at (39.0, 75.0)
- removed the REF** at (37.0, 75.0)
- removed the REF** at (35.0, 75.0)
- removed the REF** at (33.0, 75.0)
- removed the REF** at (31.0, 75.0)
- removed the REF** at (29.0, 75.0)
- removed the REF** at (27.0, 75.0)
- removed the REF** at (25.0, 75.0)
- removed the REF** at (23.0, 75.0)
- removed the REF** at (111.0, 75.0)
- removed the REF** at (21.0, 75.0)
- removed the REF** at (109.0, 75.0)
- removed the REF** at (107.0, 75.0)
- removed the REF** at (105.0, 75.0)
- removed the REF** at (103.0, 75.0)
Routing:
- net GND: vias 410 -> 509
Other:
- board text added: "PS_ Feedback"
- board text removed: "PS_Feedback"
